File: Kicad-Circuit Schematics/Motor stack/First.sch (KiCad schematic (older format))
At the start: 10 parts, among them IC1 L293D, K1 CONN_3, P1 CONN_20X2, P2 CONN_2, P3 CONN_2, U1 MCP23017

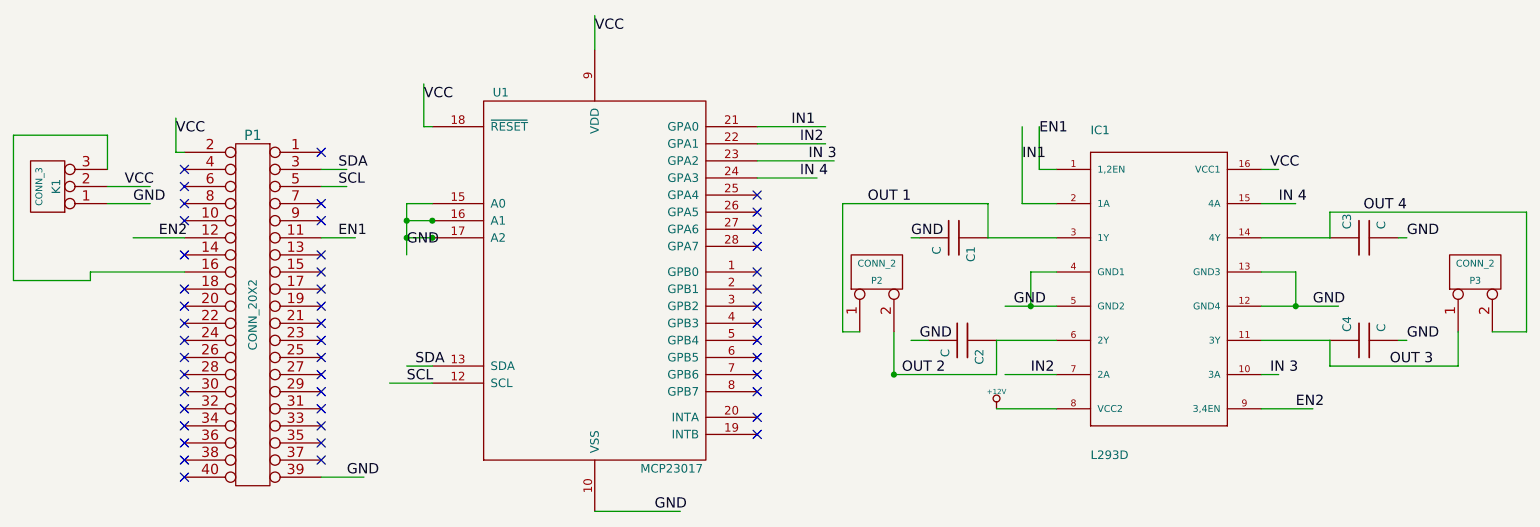
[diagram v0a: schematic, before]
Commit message: Final designs added
Contains the pcb layout and schematics of 3 stacks
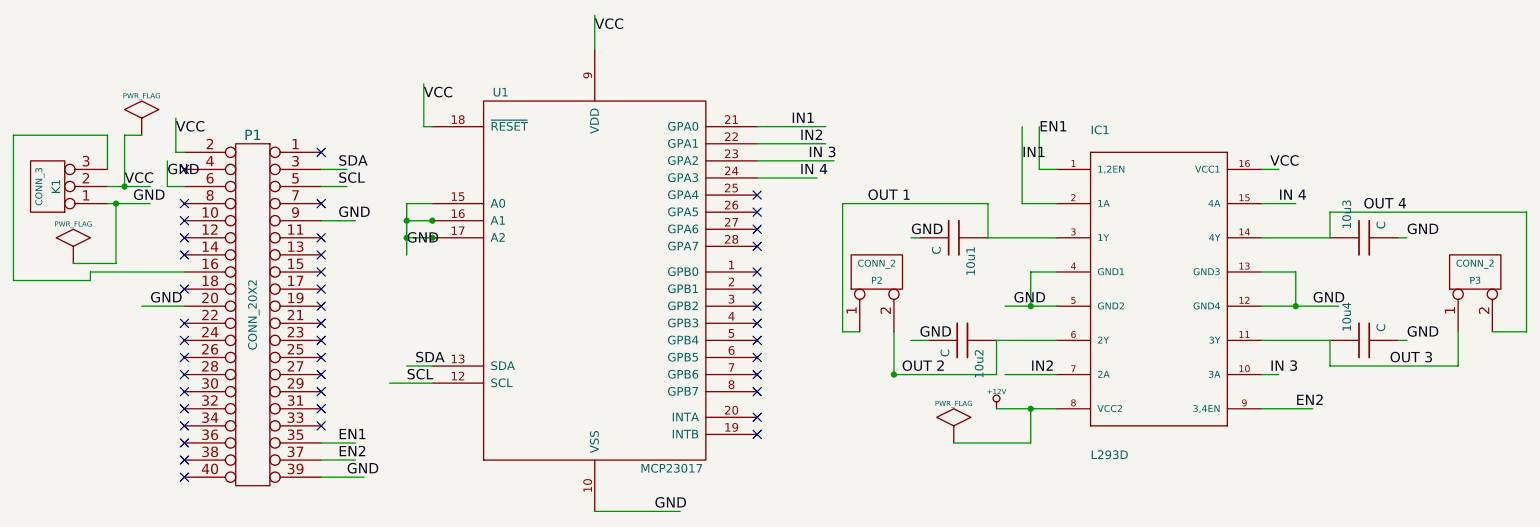
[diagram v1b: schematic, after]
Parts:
- renumbered C1 to 10u1, C2 to 10u2, C3 to 10u3, C4 to 10u4
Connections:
- wire segments 67 -> 77
- no-connect marks 47 -> 44
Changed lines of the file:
@@
-EESchema Schematic File Version 2  date 26/06/2015 16:07:03
+EESchema Schematic File Version 2  date 07/07/2015 21:11:46
 LIBS:power
 LIBS:device
@@
 Sheet 1 1
 Title "Motor driver"
-Date "26 jun 2015"
+Date "7 jul 2015"
 Rev ""
 Comp ""
@@
 Comment4 ""
 $EndDescr
-Text Label 2650 4800 0    60   ~ 0
-GND
+Text Label 2600 3300 0    60   ~ 0
+GND
+Wire Wire Line
+	2500 3300 2700 3300
+Wire Wire Line
+	1700 3800 1450 3800
+Connection ~ 1300 3200
+Wire Wire Line
+	1300 3200 1300 3550
+Wire Wire Line
+	1300 3550 1050 3550
 Wire Wire Line
 	2500 4800 2750 4800
@@
 	8000 4200 8100 4200
 Wire Wire Line
-	1700 3400 1400 3400
-Wire Wire Line
 	8300 4400 8000 4400
 Wire Wire Line
@@
 	6600 3200 6600 2750
 Wire Wire Line
-	2500 3400 2700 3400
+	2500 4600 2700 4600
 Wire Wire Line
 	8200 3200 8000 3200
@@
 Wire Wire Line
 	6700 3000 6700 2750
+Wire Wire Line
+	6200 4600 6650 4600
+Wire Wire Line
+	6650 4600 6650 4400
+Connection ~ 6650 4400
+Wire Wire Line
+	1450 2800 1350 2800
+Wire Wire Line
+	1350 2800 1350 3100
+Connection ~ 1350 3100
+Wire Wire Line
+	2500 4700 2700 4700
+Wire Wire Line
+	1700 3100 1600 3100
+Wire Wire Line
+	1600 3100 1600 2950
+Text Label 1600 3050 0    60   ~ 0
+GND
+NoConn ~ 2500 3500
+NoConn ~ 2500 3400
+$Comp
+L CONN_20X2 P1
+U 1 1 558BDC67
+P 2100 3850
+F 0 "P1" H 2100 4900 60  0000 C CNN
+F 1 "CONN_20X2" V 2100 3850 50  0000 C CNN
+	1    2100 3850
+	-1   0    0    -1
+$EndComp
+Text Label 1500 3800 0    60   ~ 0
+GND
+Text Label 2600 4700 0    60   ~ 0
+EN2
+NoConn ~ 1700 3400
+$Comp
+L PWR_FLAG #FLG01
+U 1 1 5592D22B
+P 1050 3550
+F 0 "#FLG01" H 1050 3820 30  0001 C CNN
+F 1 "PWR_FLAG" H 1050 3780 30  0000 C CNN
+	1    1050 3550
+	1    0    0    -1
+$EndComp
+$Comp
+L PWR_FLAG #FLG02
+U 1 1 5592D222
+P 1450 2800
+F 0 "#FLG02" H 1450 3070 30  0001 C CNN
+F 1 "PWR_FLAG" H 1450 3030 30  0000 C CNN
+	1    1450 2800
+	1    0    0    -1
+$EndComp
+$Comp
+L PWR_FLAG #FLG03
+U 1 1 5592D1AA
+P 6200 4600
+F 0 "#FLG03" H 6200 4870 30  0001 C CNN
+F 1 "PWR_FLAG" H 6200 4830 30  0000 C CNN
+	1    6200 4600
+	1    0    0    -1
+$EndComp
+Text Label 2650 4800 0    60   ~ 0
+GND
 Text Label 6700 2800 0    60   ~ 0
 EN1
@@
 NoConn ~ 2500 2900
 Text Label 8200 4400 0    60   ~ 0
-EN2
-Text Label 1550 3400 0    60   ~ 0
 EN2
 Text Label 5300 3050 0    60   ~ 0
@@
 Text Label 8050 3000 0    60   ~ 0
 VCC
-Text Label 2600 3400 0    60   ~ 0
+Text Label 2600 4600 0    60   ~ 0
 EN1
 Text Label 2600 3100 0    60   ~ 0
@@
 NoConn ~ 1700 3300
 NoConn ~ 1700 3200
-NoConn ~ 1700 3100
 NoConn ~ 1700 3000
 NoConn ~ 2500 3200
-NoConn ~ 2500 3300
-NoConn ~ 2500 3500
 NoConn ~ 2500 3600
 NoConn ~ 2500 3700
@@
 NoConn ~ 2500 4400
 NoConn ~ 2500 4500
-NoConn ~ 2500 4600
-NoConn ~ 2500 4700
 NoConn ~ 1700 4800
 NoConn ~ 1700 4700
@@
 NoConn ~ 1700 4000
 NoConn ~ 1700 3900
-NoConn ~ 1700 3800
 NoConn ~ 1700 3700
 NoConn ~ 1700 3500
@@
 NoConn ~ 5050 3600
 $Comp
-L +12V #PWR01
+L +12V #PWR04
 U 1 1 558CEE64
 P 6450 4400
-F 0 "#PWR01" H 6450 4350 20  0001 C CNN
+F 0 "#PWR04" H 6450 4350 20  0001 C CNN
 F 1 "+12V" H 6450 4500 30  0000 C CNN
 	1    6450 4400
@@
 $EndComp
 $Comp
-L C C4
+L C 10u4
 U 1 1 558CEB67
 P 8600 4000
-F 0 "C4" H 8650 4100 50  0000 L CNN
+F 0 "10u4" H 8650 4100 50  0000 L CNN
 F 1 "C" H 8650 3900 50  0000 L CNN
 	1    8600 4000
@@
 $EndComp
 $Comp
-L C C3
+L C 10u3
 U 1 1 558CEB52
 P 8600 3400
-F 0 "C3" H 8650 3500 50  0000 L CNN
+F 0 "10u3" H 8650 3500 50  0000 L CNN
 F 1 "C" H 8650 3300 50  0000 L CNN
 	1    8600 3400
@@
 $EndComp
 $Comp
-L C C2
+L C 10u2
 U 1 1 558CEABB
 P 6250 4000
-F 0 "C2" H 6300 4100 50  0000 L CNN
+F 0 "10u2" H 6300 4100 50  0000 L CNN
 F 1 "C" H 6300 3900 50  0000 L CNN
 	1    6250 4000
@@
 $EndComp
 $Comp
-L C C1
+L C 10u1
 U 1 1 558CEA94
 P 6200 3400
-F 0 "C1" H 6250 3500 50  0000 L CNN
+F 0 "10u1" H 6250 3500 50  0000 L CNN
 F 1 "C" H 6250 3300 50  0000 L CNN
 	1    6200 3400
@@
 	1    0    0    -1
 $EndComp
-$Comp
-L CONN_20X2 P1
-U 1 1 558BDC67
-P 2100 3850
-F 0 "P1" H 2100 4900 60  0000 C CNN
-F 1 "CONN_20X2" V 2100 3850 50  0000 C CNN
-	1    2100 3850
-	-1   0    0    -1
-$EndComp
 $EndSCHEMATC
